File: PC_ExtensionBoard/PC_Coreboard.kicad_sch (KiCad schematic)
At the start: 1 part, among them U3 KBLH-E61_COMe_Type6_16U

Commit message: update schematic: add pattern
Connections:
- net USB_6_7_OC#: now reaches U3.A38 (USB_6_7_OC#)
- net USB_2_3_OC#: now reaches U3.A44 (USB_2_3_OC#)
- net USB_4_5_OC#: now reaches U3.B38 (USB_4_5_OC#)
- net USB_0_1_OC#: now reaches U3.B44 (USB_0_1_OC#)
- net GND: now reaches U3.A1 (GND)
- net GND: now also U3.A11 (GND), U3.A110 (GND), U3.A21 (GND), U3.A31 (GND), U3.A41 (GND), U3.A51 (GND), U3.A57 (GND), U3.A60 (GND), U3.A66 (GND), U3.A70 (GND), U3.A80 (GND), U3.A90 (GND), U3.B1 (GND), U3.B11 (GND), U3.B110 (GND), U3.B21 (GND), U3.B31 (GND), U3.B41 (GND), U3.B51 (GND), U3.B60 (GND), U3.B70 (GND), U3.B80 (GND), U3.B90 (GND), U3.C1 (GND), U3.C100 (GND), U3.C103 (GND), U3.C11 (GND), U3.C110 (GND), U3.C14 (GND), U3.C2 (GND), U3.C21 (GND), U3.C31 (GND), U3.C41 (GND), U3.C5 (GND), U3.C51 (GND), U3.C60 (GND), U3.C67 (GND), U3.C70 (GND), U3.C73 (GND), U3.C76 (GND), U3.C8 (GND), U3.C84 (GND), U3.C87 (GND), U3.C90 (GND), U3.C93 (GND), U3.C96 (GND), U3.D1 (GND), U3.D100 (GND), U3.D103 (GND), U3.D11 (GND), U3.D110 (GND), U3.D14 (GND), U3.D2 (GND), U3.D21 (GND), U3.D31 (GND), U3.D41 (GND), U3.D5 (GND), U3.D51 (GND), U3.D60 (GND), U3.D67 (GND), U3.D70 (GND), U3.D73 (GND), U3.D76 (GND), U3.D8 (GND), U3.D80 (GND), U3.D84 (GND), U3.D87 (GND), U3.D90 (GND), U3.D93 (GND), U3.D96 (GND)
- net VCC_12V: now reaches U3.A104 (VCC_12V)
- net VCC_12V: now also U3.A105 (VCC_12V), U3.A106 (VCC_12V), U3.A107 (VCC_12V), U3.A108 (VCC_12V), U3.A109 (VCC_12V), U3.B104 (VCC_12V), U3.B105 (VCC_12V), U3.B106 (VCC_12V), U3.B107 (VCC_12V), U3.B108 (VCC_12V), U3.B109 (VCC_12V), U3.C104 (VCC_12V), U3.C105 (VCC_12V), U3.C106 (VCC_12V), U3.C107 (VCC_12V), U3.C108 (VCC_12V), U3.C109 (VCC_12V), U3.D104 (VCC_12V), U3.D105 (VCC_12V), U3.D106 (VCC_12V), U3.D107 (VCC_12V), U3.D108 (VCC_12V), U3.D109 (VCC_12V)
- net at U3.B84 (VCC_5V_SBY): now also U3.B85 (VCC_5V_SBY), U3.B86 (VCC_5V_SBY), U3.B87 (VCC_5V_SBY)
- net GBE0.MDI1+: now reaches U3.A10 (GBE0_MDI1+)
- net GBE0.MDI0-: now reaches U3.A12 (GBE0_MDI0-)
- net GBE0.MDI0+: now reaches U3.A13 (GBE0_MDI0+)
- net GBE0.CTREF: now reaches U3.A14 (GBE0_CTREF)
- net GBE0.MDI3-: now reaches U3.A2 (GBE0_MDI3-)
- net GBE0.MDI3+: now reaches U3.A3 (GBE0_MDI3+)
- net ~{GBE0_LINK_1000}: now reaches U3.A5 (GBE0_LINK1000#)
- net GBE0.MDI2-: now reaches U3.A6 (GBE0_MDI2-)
- net GBE0.MDI2+: now reaches U3.A7 (GBE0_MDI2+)
- net ~{GBE0_LINK}: now reaches U3.A8 (GBE0_LINK#)
- net GBE0.MDI1-: now reaches U3.A9 (GBE0_MDI1-)
- net ~{GBE0_ACT}: now reaches U3.B2 (GBE0_ACT#)
- net PCIe_{B1x2}.RX1+: now reaches U3.A52 (PCIE_TX5+)
- net PCIe_{B1x2}.RX1-: now reaches U3.A53 (PCIE_TX5-)
- net PCIe_{B1x2}.RX0+: now reaches U3.A55 (PCIE_TX4+)
- net PCIe_{B1x2}.RX0-: now reaches U3.A56 (PCIE_TX4-)
- net PCIe_{B1x4}.RX3+: now reaches U3.A58 (PCIE_TX3+)
- net PCIe_{B1x4}.RX3-: now reaches U3.A59 (PCIE_TX3-)
- net PCIe_{B1x4}.RX2+: now reaches U3.A61 (PCIE_TX2+)
- net PCIe_{B1x4}.RX2-: now reaches U3.A62 (PCIE_TX2-)
- net PCIe_{B1x4}.RX1+: now reaches U3.A64 (PCIE_TX1+)
- net PCIe_{B1x4}.RX1-: now reaches U3.A65 (PCIE_TX1-)
- net PCIe_{B1x4}.RX0+: now reaches U3.A68 (PCIE_TX0+)
- net PCIe_{B1x4}.RX0-: now reaches U3.A69 (PCIE_TX0-)
- net PCIe_{B1x2}.TX1+: now reaches U3.B52 (PCIE_RX5+)
- net PCIe_{B1x2}.TX1-: now reaches U3.B53 (PCIE_RX5-)
- net PCIe_{B1x2}.TX0+: now reaches U3.B55 (PCIE_RX4+)
- net PCIe_{B1x2}.TX0-: now reaches U3.B56 (PCIE_RX4-)
- net PCIe_{B1x4}.TX3+: now reaches U3.B58 (PCIE_RX3+)
- net PCIe_{B1x4}.TX3-: now reaches U3.B59 (PCIE_RX3-)
- net PCIe_{B1x4}.TX2+: now reaches U3.B61 (PCIE_RX2+)
- net PCIe_{B1x4}.TX2-: now reaches U3.B62 (PCIE_RX2-)
- net PCIe_{B1x4}.TX1+: now reaches U3.B64 (PCIE_RX1+)
- net PCIe_{B1x4}.TX1-: now reaches U3.B65 (PCIE_RX1-)
- net PCIe_{B1x4}.TX0+: now reaches U3.B68 (PCIE_RX0+)
- net PCIe_{B1x4}.TX0-: now reaches U3.B69 (PCIE_RX0-)
- no-connect marks 0 -> 1

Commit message: components placement R1
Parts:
- added H10, H11, H12, H13, H6, H7, H8, H9: Spacer_Drill3.7mm_H2.5mm_9774025151R, PC_Components_1:Spacer_Drill3.7mm_H2.5mm_9774025151R, symbol antmicroMechanicalParts:Spacer_Drill3.7mm_H2.5mm_9774025151R
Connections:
- net GND: now also H10.1, H11.1, H12.1, H13.1, H6.1, H7.1, H8.1, H9.1
- net PCIE_{REF}.CK+: now reaches U3.A88 (PCIE_CLK+)
- net PCIE_{REF}.CK-: now reaches U3.A89 (PCIE_CLK-)

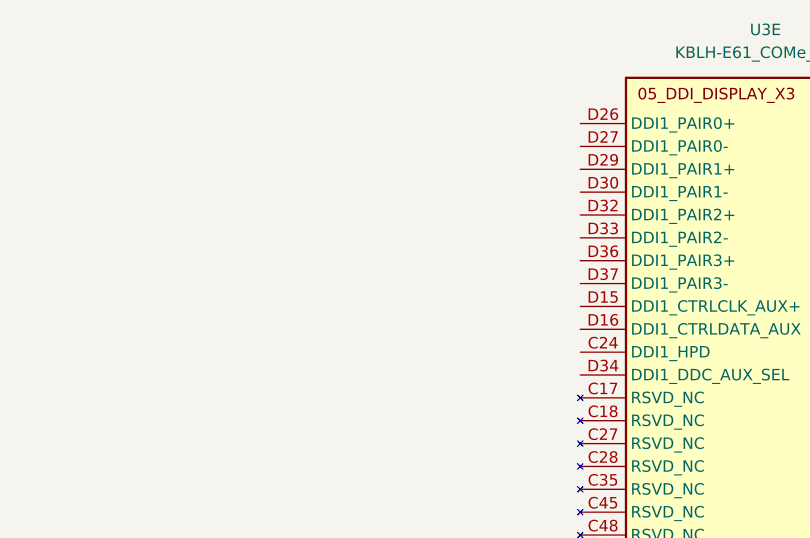
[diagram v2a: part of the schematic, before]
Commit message: update schematic
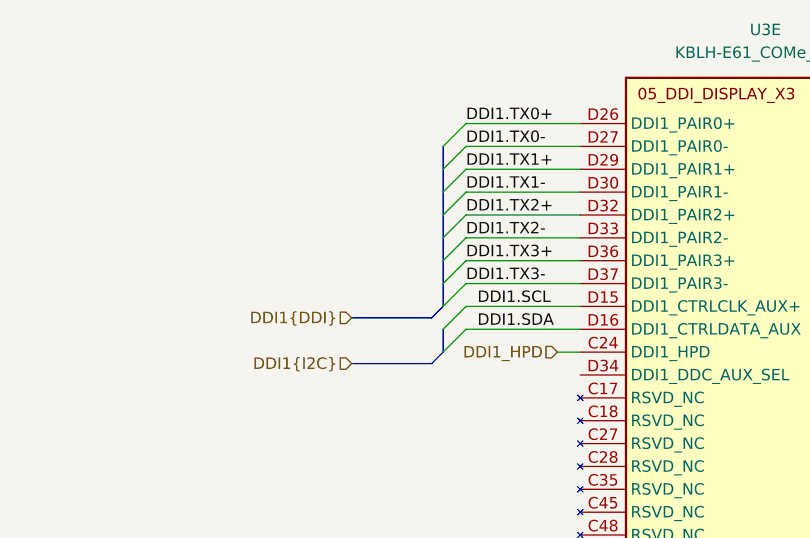
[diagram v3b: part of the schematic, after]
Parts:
- U3: LCSC (none) -> C2761498
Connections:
- net DDI1_HPD: now reaches U3.C24 (DDI1_HPD)
- net DDI1.SCL: now reaches U3.D15 (DDI1_CTRLCLK_AUX+)
- net DDI1.SDA: now reaches U3.D16 (DDI1_CTRLDATA_AUX)
- net DDI1.TX0+: now reaches U3.D26 (DDI1_PAIR0+)
- net DDI1.TX0-: now reaches U3.D27 (DDI1_PAIR0-)
- net DDI1.TX1+: now reaches U3.D29 (DDI1_PAIR1+)
- net DDI1.TX1-: now reaches U3.D30 (DDI1_PAIR1-)
- net DDI1.TX2+: now reaches U3.D32 (DDI1_PAIR2+)
- net DDI1.TX2-: now reaches U3.D33 (DDI1_PAIR2-)
- net DDI1.TX3+: now reaches U3.D36 (DDI1_PAIR3+)
- net DDI1.TX3-: now reaches U3.D37 (DDI1_PAIR3-)

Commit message: refactor project
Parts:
- removed H10, H11, H12, H13, H6, H7, H8, H9: Spacer_Drill3.7mm_H2.5mm_9774025151R, PC_Components_1:Spacer_Drill3.7mm_H2.5mm_9774025151R, symbol antmicroMechanicalParts:Spacer_Drill3.7mm_H2.5mm_9774025151R
- removed U3: KBLH-E61_COMe_Type6_16U, DatCao_FootPrint:CORE_BOARD_CUSTOM_440_PIN, symbol DatCao_Symbol:KBLH-E61_COMe_Type6_16U
- added H2: Spacer_Drill3.7mm_H5mm_9774025151R, symbol A_PC_ExtensionBoard:Spacer_Drill3.7mm_H5mm_9774025151R
- added U3: KBLH-E61_COMe_Type6_16U, DatCao_FootPrint:CORE_BOARD_CUSTOM_440_PIN, symbol A_PC_ExtensionBoard:KBLH-E61_COMe_Type6_16U
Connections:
- net DDI1.SCL: now also U3.D15 (DDI1_CTRLCLK_AUX+)
- net DDI1.SDA: now also U3.D16 (DDI1_CTRLDATA_AUX)
- net DDI1.TX0+: now also U3.D26 (DDI1_PAIR0+)
- net DDI1.TX0-: now also U3.D27 (DDI1_PAIR0-)
- net DDI1.TX1+: now also U3.D29 (DDI1_PAIR1+)
- net DDI1.TX1-: now also U3.D30 (DDI1_PAIR1-)
- net DDI1.TX2+: now also U3.D32 (DDI1_PAIR2+)
- net DDI1.TX2-: now also U3.D33 (DDI1_PAIR2-)
- net DDI1.TX3+: now also U3.D36 (DDI1_PAIR3+)
- net DDI1.TX3-: now also U3.D37 (DDI1_PAIR3-)
- net DDI1_HPD: now also U3.C24 (DDI1_HPD)
- net GBE0.CTREF: now also U3.A14 (GBE0_CTREF)
- net GBE0.MDI0+: now also U3.A13 (GBE0_MDI0+)
- net GBE0.MDI0-: now also U3.A12 (GBE0_MDI0-)
- net GBE0.MDI1+: now also U3.A10 (GBE0_MDI1+)
- net GBE0.MDI1-: now also U3.A9 (GBE0_MDI1-)
- net GBE0.MDI2+: now also U3.A7 (GBE0_MDI2+)
- net GBE0.MDI2-: now also U3.A6 (GBE0_MDI2-)
- net GBE0.MDI3+: now also U3.A3 (GBE0_MDI3+)
- net GBE0.MDI3-: now also U3.A2 (GBE0_MDI3-)
- net GND: now also H2.1, U3.A1 (GND), U3.A11 (GND), U3.A110 (GND), U3.A21 (GND), U3.A31 (GND), U3.A41 (GND), U3.A51 (GND), U3.A57 (GND), U3.A60 (GND), U3.A66 (GND), U3.A70 (GND), U3.A80 (GND), U3.A90 (GND), U3.B1 (GND), U3.B11 (GND), U3.B110 (GND), U3.B21 (GND), U3.B31 (GND), U3.B41 (GND), U3.B51 (GND), U3.B60 (GND), U3.B70 (GND), U3.B80 (GND), U3.B90 (GND), U3.C1 (GND), U3.C100 (GND), U3.C103 (GND), U3.C11 (GND), U3.C110 (GND), U3.C14 (GND), U3.C2 (GND), U3.C21 (GND), U3.C31 (GND), U3.C41 (GND), U3.C5 (GND), U3.C51 (GND), U3.C60 (GND), U3.C67 (GND), U3.C70 (GND), U3.C73 (GND), U3.C76 (GND), U3.C8 (GND), U3.C84 (GND), U3.C87 (GND), U3.C90 (GND), U3.C93 (GND), U3.C96 (GND), U3.D1 (GND), U3.D100 (GND), U3.D103 (GND), U3.D11 (GND), U3.D110 (GND), U3.D14 (GND), U3.D2 (GND), U3.D21 (GND), U3.D31 (GND), U3.D41 (GND), U3.D5 (GND), U3.D51 (GND), U3.D60 (GND), U3.D67 (GND), U3.D70 (GND), U3.D73 (GND), U3.D76 (GND), U3.D8 (GND), U3.D80 (GND), U3.D84 (GND), U3.D87 (GND), U3.D90 (GND), U3.D93 (GND), U3.D96 (GND)
- net PCIE_{REF}.CK+: now also U3.A88 (PCIE_CLK+)
- net PCIE_{REF}.CK-: now also U3.A89 (PCIE_CLK-)
- net PCIe_{B1x2}.RX0+: now also U3.A55 (PCIE_TX4+)
- net PCIe_{B1x2}.RX0-: now also U3.A56 (PCIE_TX4-)
- net PCIe_{B1x2}.RX1+: now also U3.A52 (PCIE_TX5+)
- net PCIe_{B1x2}.RX1-: now also U3.A53 (PCIE_TX5-)
- net PCIe_{B1x2}.TX0+: now also U3.B55 (PCIE_RX4+)
- net PCIe_{B1x2}.TX0-: now also U3.B56 (PCIE_RX4-)
- net PCIe_{B1x2}.TX1+: now also U3.B52 (PCIE_RX5+)
- net PCIe_{B1x2}.TX1-: now also U3.B53 (PCIE_RX5-)
- net PCIe_{B1x4}.RX0+: now also U3.A68 (PCIE_TX0+)
- net PCIe_{B1x4}.RX0-: now also U3.A69 (PCIE_TX0-)
- net PCIe_{B1x4}.RX1+: now also U3.A64 (PCIE_TX1+)
- net PCIe_{B1x4}.RX1-: now also U3.A65 (PCIE_TX1-)
- net PCIe_{B1x4}.RX2+: now also U3.A61 (PCIE_TX2+)
- net PCIe_{B1x4}.RX2-: now also U3.A62 (PCIE_TX2-)
- net PCIe_{B1x4}.RX3+: now also U3.A58 (PCIE_TX3+)
- net PCIe_{B1x4}.RX3-: now also U3.A59 (PCIE_TX3-)
- net PCIe_{B1x4}.TX0+: now also U3.B68 (PCIE_RX0+)
- net PCIe_{B1x4}.TX0-: now also U3.B69 (PCIE_RX0-)
- net PCIe_{B1x4}.TX1+: now also U3.B64 (PCIE_RX1+)
- net PCIe_{B1x4}.TX1-: now also U3.B65 (PCIE_RX1-)
- net PCIe_{B1x4}.TX2+: now also U3.B61 (PCIE_RX2+)
- net PCIe_{B1x4}.TX2-: now also U3.B62 (PCIE_RX2-)
- net PCIe_{B1x4}.TX3+: now also U3.B58 (PCIE_RX3+)
- net PCIe_{B1x4}.TX3-: now also U3.B59 (PCIE_RX3-)
- net USB0.D+: now also U3.A46 (USB0+)
- net USB0.D-: now also U3.A45 (USB0-)
- net USB1.D+: now also U3.B46 (USB1+)
- net USB1.D-: now also U3.B45 (USB1-)
- net USB2.D+: now also U3.A43 (USB2+)
- net USB2.D-: now also U3.A42 (USB2-)
- net USB3.D+: now also U3.B43 (USB3+)
- net USB3.D-: now also U3.B42 (USB3-)
- net USB4.D+: now also U3.A40 (USB4+)
- net USB4.D-: now also U3.A39 (USB4-)
- net USB5.D+: now also U3.B40 (USB5+)
- net USB5.D-: now also U3.B39 (USB5-)
- net USB6.D+: now also U3.A37 (USB6+)
- net USB6.D-: now also U3.A36 (USB6-)
- net USB7.D+: now also U3.B37 (USB7+)
- net USB7.D-: now also U3.B36 (USB7-)
- net USBSS0.RX+: now also U3.C4 (USB_SSRX0+)
- net USBSS0.RX-: now also U3.C3 (USB_SSRX0-)
- net USBSS0.TX+: now also U3.D4 (USB_SSTX0+)
- net USBSS0.TX-: now also U3.D3 (USB_SSTX0-)
- net USBSS1.RX+: now also U3.C7 (USB_SSRX1+)
- net USBSS1.RX-: now also U3.C6 (USB_SSRX1-)
- net USBSS1.TX+: now also U3.D7 (USB_SSTX1+)
- net USBSS1.TX-: now also U3.D6 (USB_SSTX1-)
- net USBSS2.RX+: now also U3.C10 (USB_SSRX2+)
- net USBSS2.RX-: now also U3.C9 (USB_SSRX2-)
- net USBSS2.TX+: now also U3.D10 (USB_SSTX2+)
- net USBSS2.TX-: now also U3.D9 (USB_SSTX2-)
- net USBSS3.RX+: now also U3.C13 (USB_SSRX3+)
- net USBSS3.RX-: now also U3.C12 (USB_SSRX3-)
- net USBSS3.TX+: now also U3.D13 (USB_SSTX3+)
- net USBSS3.TX-: now also U3.D12 (USB_SSTX3-)
- net USB_0_1_OC#: now also U3.B44 (USB_0_1_OC#)
- net USB_2_3_OC#: now also U3.A44 (USB_2_3_OC#)
- net USB_4_5_OC#: now also U3.B38 (USB_4_5_OC#)
- net USB_6_7_OC#: now also U3.A38 (USB_6_7_OC#)
- net VCC_12V: now also U3.A104 (VCC_12V), U3.A105 (VCC_12V), U3.A106 (VCC_12V), U3.A107 (VCC_12V), U3.A108 (VCC_12V), U3.A109 (VCC_12V), U3.B104 (VCC_12V), U3.B105 (VCC_12V), U3.B106 (VCC_12V), U3.B107 (VCC_12V), U3.B108 (VCC_12V), U3.B109 (VCC_12V), U3.C104 (VCC_12V), U3.C105 (VCC_12V), U3.C106 (VCC_12V), U3.C107 (VCC_12V), U3.C108 (VCC_12V), U3.C109 (VCC_12V), U3.D104 (VCC_12V), U3.D105 (VCC_12V), U3.D106 (VCC_12V), U3.D107 (VCC_12V), U3.D108 (VCC_12V), U3.D109 (VCC_12V)
- net ~{GBE0_ACT}: now also U3.B2 (GBE0_ACT#)
- net ~{GBE0_LINK_1000}: now also U3.A5 (GBE0_LINK1000#)
- net ~{GBE0_LINK}: now also U3.A8 (GBE0_LINK#)
- new net: U3.B84 (VCC_5V_SBY), U3.B85 (VCC_5V_SBY), U3.B86 (VCC_5V_SBY), U3.B87 (VCC_5V_SBY)

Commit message: re-link symbol
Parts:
- added H3, H4, H5, H6, H7, H8, H9: Spacer_Drill3.7mm_H5mm_9774025151R, PC_Components_1:Spacer_Drill3.7mm_H5mm_9774050151R, symbol A_PC_ExtensionBoard:Spacer_Drill3.7mm_H5mm_9774025151R
- H2: footprint (none) -> PC_Components_1:Spacer_Drill3.7mm_H5mm_9774050151R
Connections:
- net GND: now also H3.1, H4.1, H5.1, H6.1, H7.1, H8.1, H9.1
- net VCC_RTC: now reaches U3.A47 (VCC_RTC)

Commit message: update LCSC for HDMI
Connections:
- net PWRBTN: now reaches U3.B12 (PWRBTN#)
- net SYNC: now reaches U3.A29 (HDA_SYNC)
- net RST: now reaches U3.A30 (HDA_RST#)
- net BITCLK: now reaches U3.A32 (HDA_BITCLK)
- net SDOUT: now reaches U3.A33 (HDA_SDOUT)
- net SDIN0: now reaches U3.B30 (HDA_SDIN0)
- net SPKR: now reaches U3.B32 (SPKR)
- no-connect marks 1 -> 3
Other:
- moved on the sheet: U3L, U3M, U3N, U3O, U3P

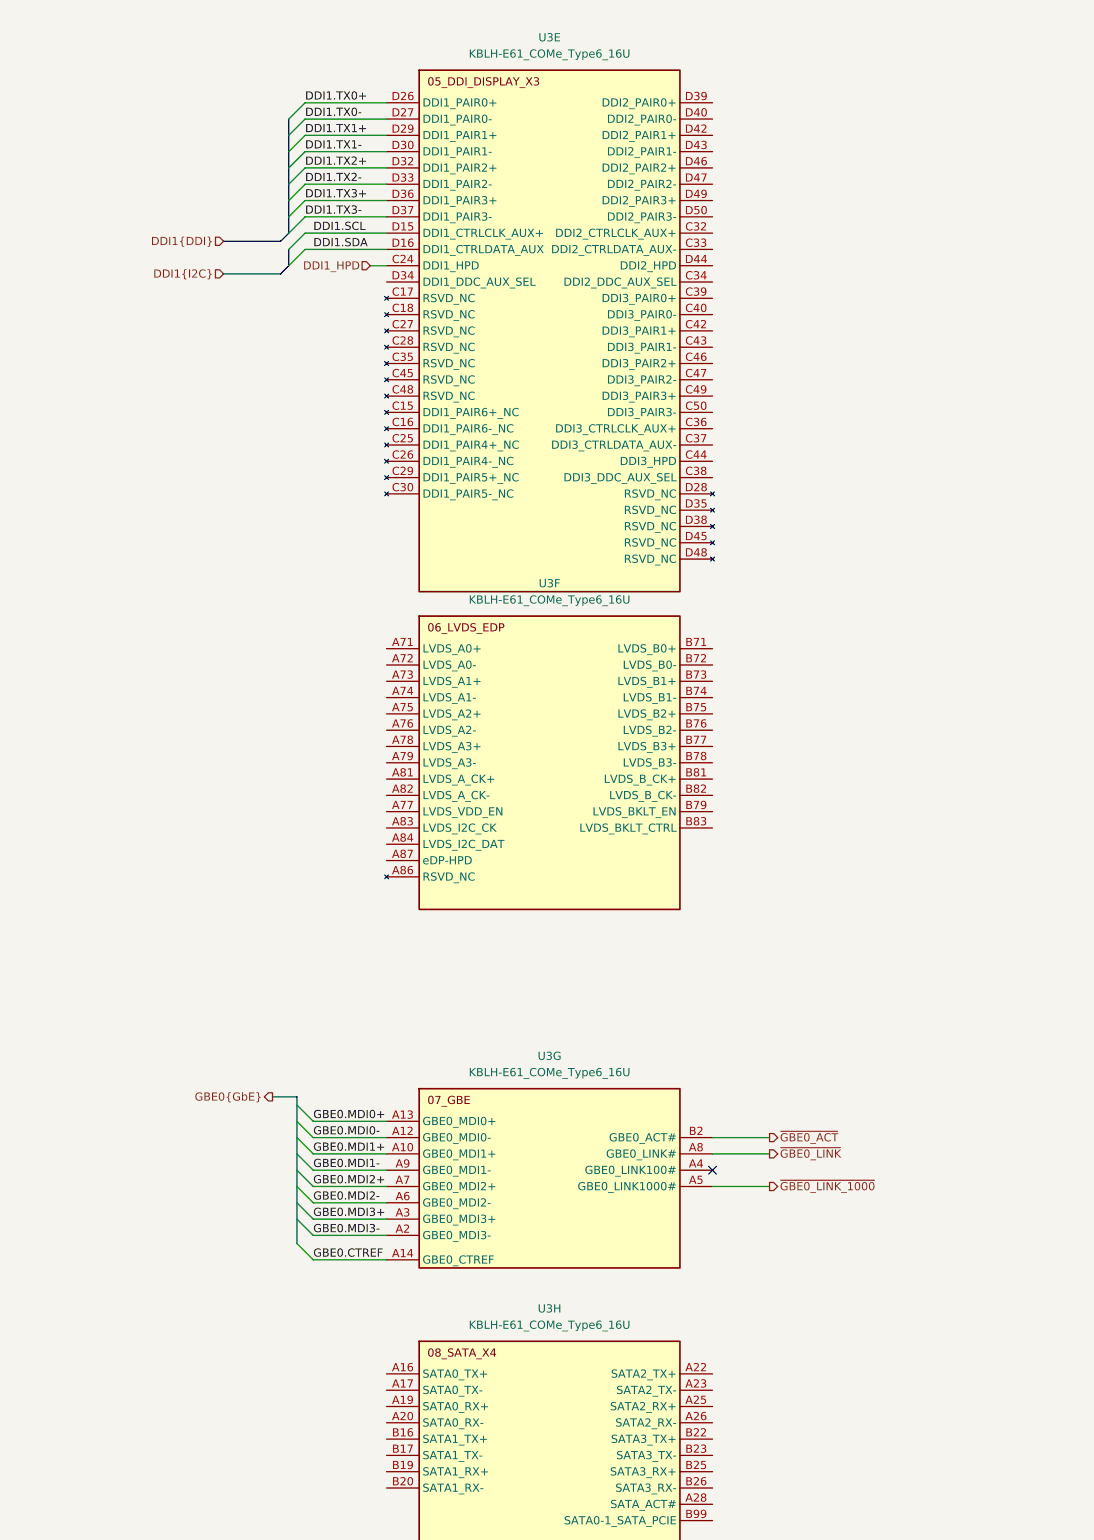
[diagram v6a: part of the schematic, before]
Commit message: update LCSC
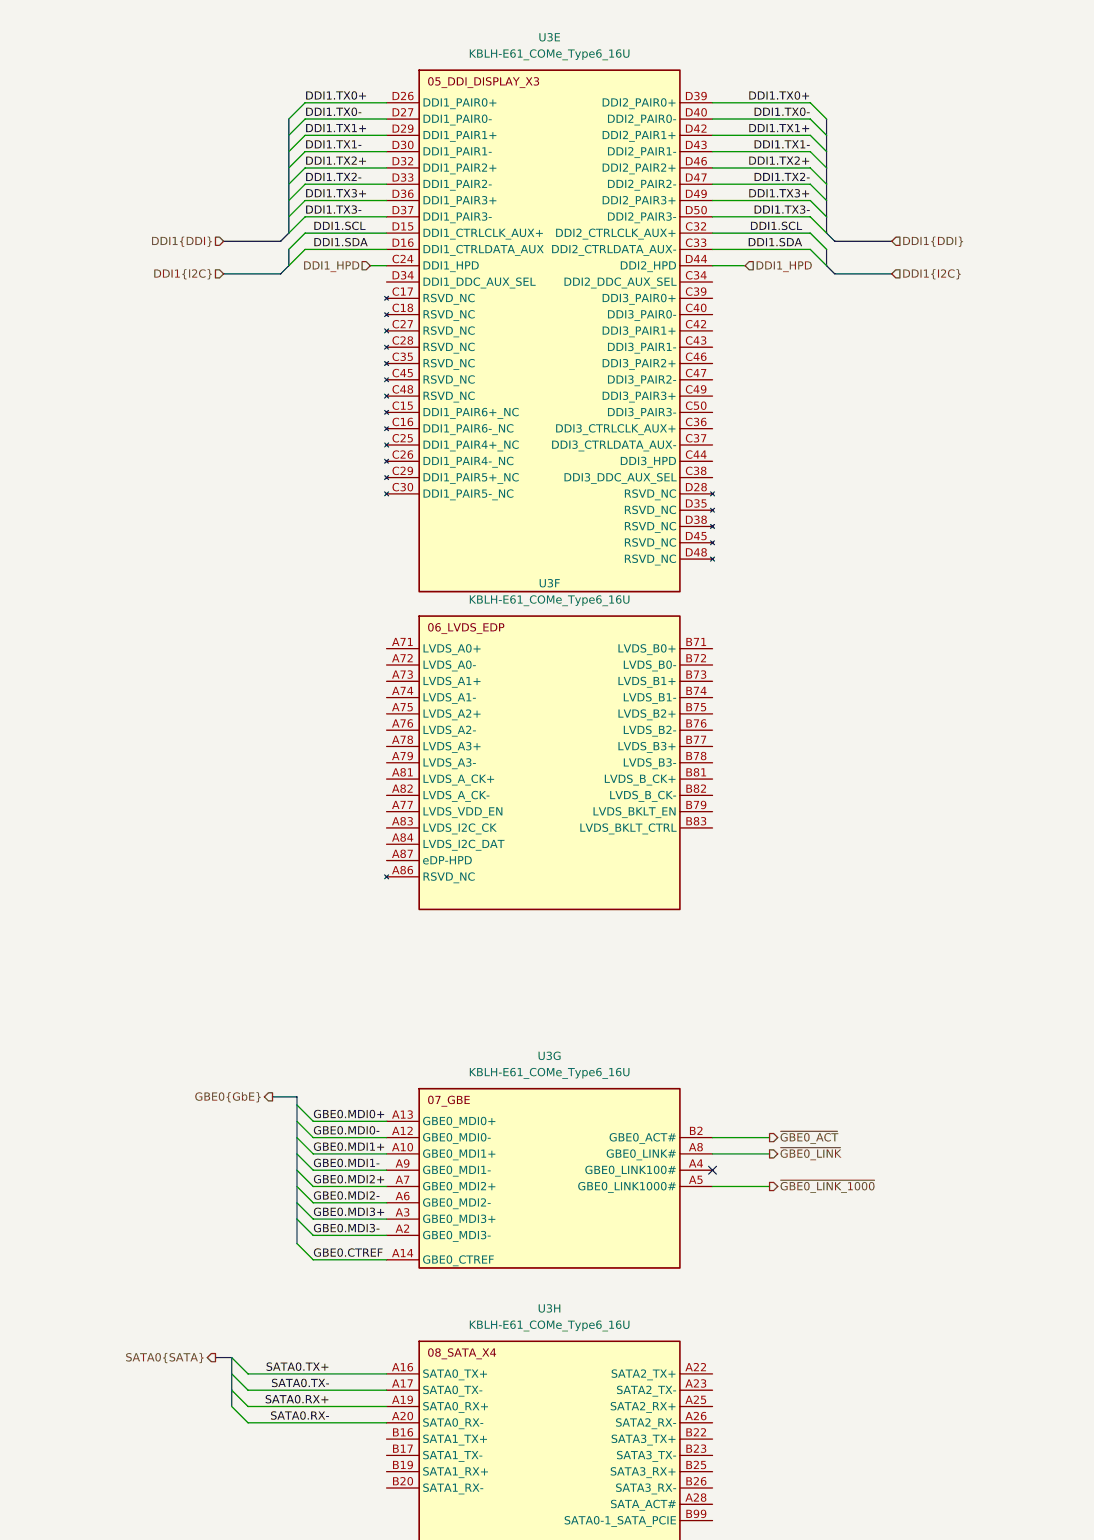
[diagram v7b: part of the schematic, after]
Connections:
- net DDI1.SCL: now also U3.C32 (DDI2_CTRLCLK_AUX+)
- net DDI1.SDA: now also U3.C33 (DDI2_CTRLDATA_AUX-)
- net DDI1.TX0+: now also U3.D39 (DDI2_PAIR0+)
- net DDI1.TX0-: now also U3.D40 (DDI2_PAIR0-)
- net DDI1.TX1+: now also U3.D42 (DDI2_PAIR1+)
- net DDI1.TX1-: now also U3.D43 (DDI2_PAIR1-)
- net DDI1.TX2+: now also U3.D46 (DDI2_PAIR2+)
- net DDI1.TX2-: now also U3.D47 (DDI2_PAIR2-)
- net DDI1.TX3+: now also U3.D49 (DDI2_PAIR3+)
- net DDI1.TX3-: now also U3.D50 (DDI2_PAIR3-)
- net DDI1_HPD: now also U3.D44 (DDI2_HPD)
- net SATA0.TX+: now reaches U3.A16 (SATA0_TX+)
- net SATA0.TX-: now reaches U3.A17 (SATA0_TX-)
- net SATA0.RX+: now reaches U3.A19 (SATA0_RX+)
- net SATA0.RX-: now reaches U3.A20 (SATA0_RX-)

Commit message: schematic changes
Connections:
- net RESETBTN: now reaches U3.B49 (SYS_RESET#)
- net DDI2_AUX_SEL: now reaches U3.C34 (DDI2_DDC_AUX_SEL)
- net DDI1_AUX_SEL: now reaches U3.D34 (DDI1_DDC_AUX_SEL)
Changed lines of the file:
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@@
 	(wire
 		(pts
+			(xy 59.69 107.95) (xy 67.31 107.95)
+		)
+		(stroke
+			(width 0)
+			(type default)
+		)
+	)
+	(wire
+		(pts
 			(xy 59.69 64.77) (xy 67.31 64.77)
 		)
@@
 	(wire
 		(pts
+			(xy 265.43 57.15) (xy 269.24 57.15)
+		)
+		(stroke
+			(width 0)
+			(type default)
+		)
+	)
+	(wire
+		(pts
 			(xy 208.28 323.85) (xy 208.28 335.28)
 		)
@@
 	(wire
 		(pts
+			(xy 212.09 57.15) (xy 214.63 57.15)
+		)
+		(stroke
+			(width 0)
+			(type default)
+		)
+	)
+	(wire
+		(pts
 			(xy 120.65 256.54) (xy 132.08 256.54)
 		)
@@
 		)
 	)
+	(hierarchical_label "DDI2_AUX_SEL"
+		(shape input)
+		(at 269.24 57.15 0)
+		(effects
+			(font
+				(size 1.27 1.27)
+			)
+			(justify left)
+		)
+	)
 	(hierarchical_label "USBSS2{USBSS}"
 		(shape output)
@@
 		)
 	)
+	(hierarchical_label "RESETBTN"
+		(shape input)
+		(at 59.69 107.95 180)
+		(effects
+			(font
+				(size 1.27 1.27)
+			)
+			(justify right)
+		)
+	)
 	(hierarchical_label "DDI1{DDI}"
 		(shape input)
@@
 		)
 	)
+	(hierarchical_label "DDI1_AUX_SEL"
+		(shape input)
+		(at 212.09 57.15 180)
+		(effects
+			(font
+				(size 1.27 1.27)
+			)
+			(justify right)
+		)
+	)
